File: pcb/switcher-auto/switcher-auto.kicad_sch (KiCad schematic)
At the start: 9 parts, among them J1 Conn_02x22_Top_Bottom, J2 Conn_02x22_Top_Bottom, J3 Conn_02x22_Top_Bottom, U1 CD74HC4067SM96, U2 CD74HC4067SM96, U3 CD74HC4067SM96, U4 CD74HC4067SM96, U5 CD74HC4067SM96, U6 CD74HC4067SM96

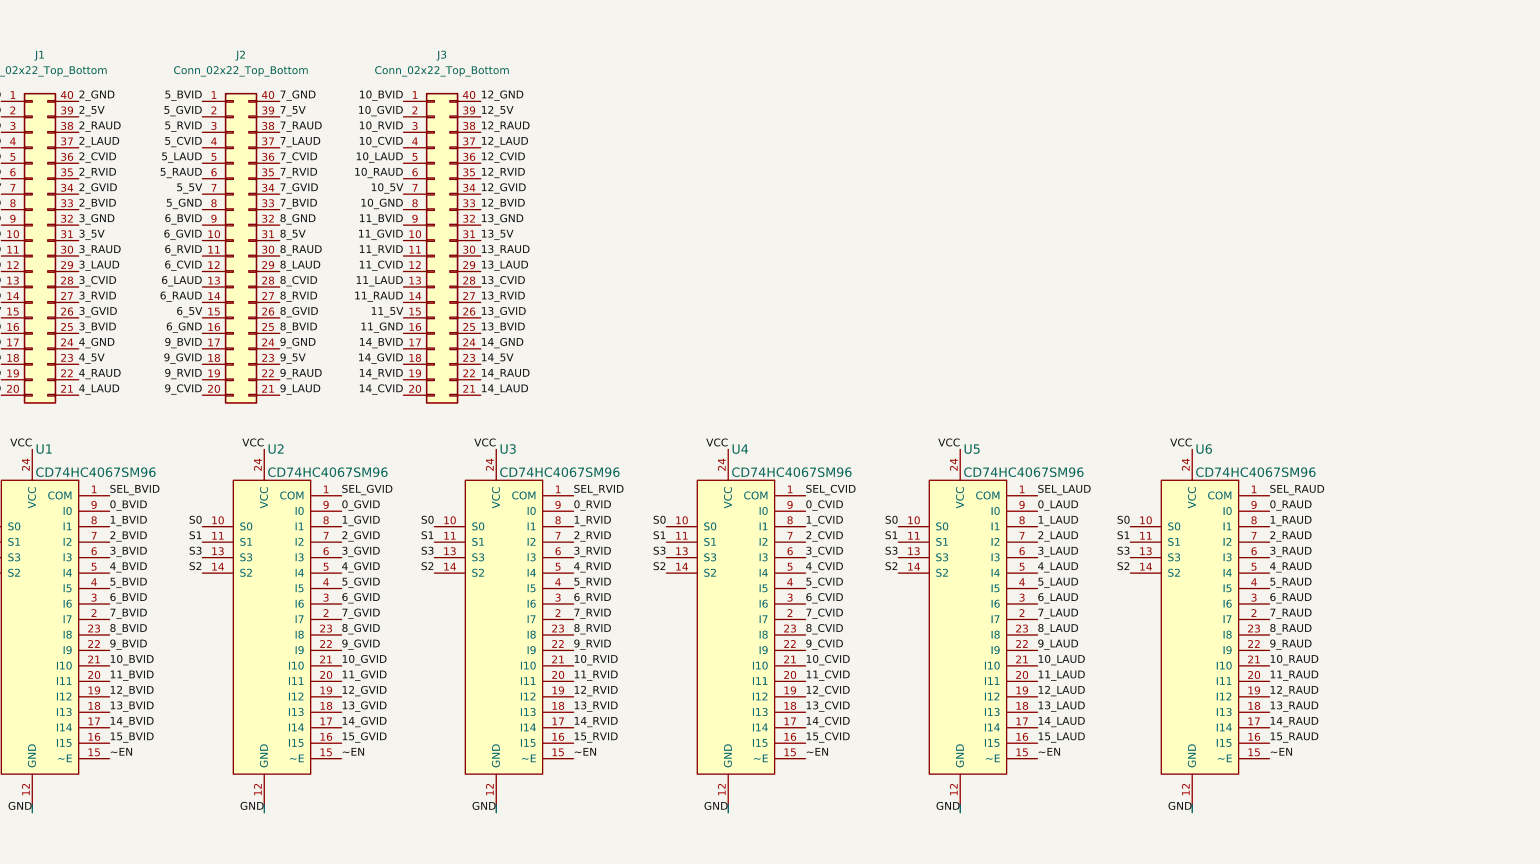
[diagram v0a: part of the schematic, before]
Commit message: autorouting 2layer switcher
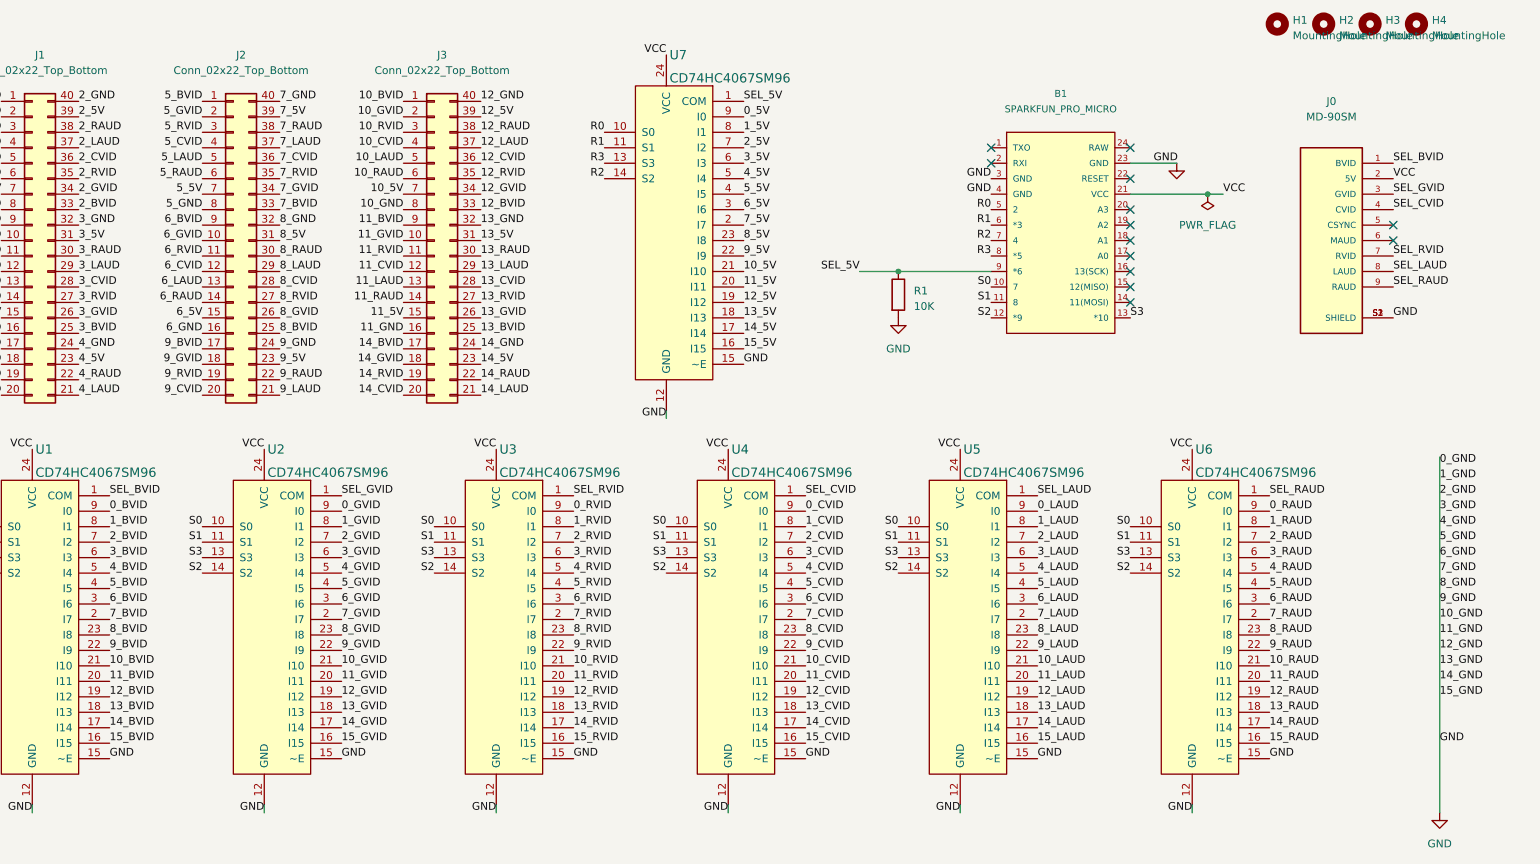
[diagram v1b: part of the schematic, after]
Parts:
- added B1: SPARKFUN_PRO_MICRO, SparkFun-Boards:SPARKFUN_PRO_MICRO, symbol SparkFun-Boards:SPARKFUN_PRO_MICRO
- added H1, H2, H3, H4: MountingHole, MountingHole:MountingHole_2.5mm, symbol Mechanical:MountingHole
- added J0: MD-90SM, DIN9:CUI_MD-90SM, symbol DIN9:MD-90SM
- added R1: 10K, Resistor_SMD:R_0805_2012Metric_Pad1.20x1.40mm_HandSolder, symbol Device:R
- added U7: CD74HC4067SM96, Package_SO:SSOP-24_5.3x8.2mm_P0.65mm, symbol dk_Interface-Analog-Switches-Multiplexers-Demultiplexers:CD74HC4067SM96
- U1, U2, U3, U4, U5, U6: footprint digikey-footprints:SSOP-24_W5.30mm -> Package_SO:SSOP-24_5.3x8.2mm_P0.65mm
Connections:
- net 0_GND is gone; now on net GND: J1.8 (Pin_8)
- net 10_GND is gone; now on net GND: J3.8 (Pin_8)
- net 11_GND is gone; now on net GND: J3.16 (Pin_16)
- net 12_GND is gone; now on net GND: J3.40 (Pin_40)
- net 13_GND is gone; now on net GND: J3.32 (Pin_32)
- net 14_GND is gone; now on net GND: J3.24 (Pin_24)
- net 1_GND is gone; now on net GND: J1.16 (Pin_16)
- net 2_GND is gone; now on net GND: J1.40 (Pin_40)
- net 3_GND is gone; now on net GND: J1.32 (Pin_32)
- net 4_GND is gone; now on net GND: J1.24 (Pin_24)
- net 5_GND is gone; now on net GND: J2.8 (Pin_8)
- net 6_GND is gone; now on net GND: J2.16 (Pin_16)
- net 7_GND is gone; now on net GND: J2.40 (Pin_40)
- net 8_GND is gone; now on net GND: J2.32 (Pin_32)
- net 9_GND is gone; now on net GND: J2.24 (Pin_24)
- net ~EN is gone; now on net GND: U1.15 (~E), U2.15 (~E), U3.15 (~E), U4.15 (~E), U5.15 (~E), U6.15 (~E)
- net 0_5V: now also U7.9 (I0)
- net 10_5V: now also U7.21 (I10)
- net 11_5V: now also U7.20 (I11)
- net 12_5V: now also U7.19 (I12)
- net 13_5V: now also U7.18 (I13)
- net 14_5V: now also U7.17 (I14)
- net 1_5V: now also U7.8 (I1)
- net 2_5V: now also U7.7 (I2)
- net 3_5V: now also U7.6 (I3)
- net 4_5V: now also U7.5 (I4)
- net 5_5V: now also U7.4 (I5)
- net 6_5V: now also U7.3 (I6)
- net 7_5V: now also U7.2 (I7)
- net 8_5V: now also U7.23 (I8)
- net 9_5V: now also U7.22 (I9)
- net GND: now also B1.23 (GND), B1.3 (GND), B1.4 (GND), J0.S1 (SHIELD), J0.S2 (SHIELD), J0.S3 (SHIELD), R1.2, U7.12 (GND), U7.15 (~E)
- net S0: now also B1.10 (7)
- net S1: now also B1.11 (8)
- net S2: now also B1.12 (*9)
- net S3: now also B1.13 (*10)
- net SEL_BVID: now also J0.1 (BVID)
- net SEL_CVID: now also J0.4 (CVID)
- net SEL_GVID: now also J0.3 (GVID)
- net SEL_LAUD: now also J0.8 (LAUD)
- net SEL_RAUD: now also J0.9 (RAUD)
- net SEL_RVID: now also J0.7 (RVID)
- net VCC: now also B1.21 (VCC), J0.2 (5V), U7.24 (VCC)
- new net 15_5V: U7.16 (I15)
- new net R0: B1.5 (2), U7.10 (S0)
- new net R1: B1.6 (*3), U7.11 (S1)
- new net R2: B1.7 (4), U7.14 (S2)
- new net R3: B1.8 (*5), U7.13 (S3)
- new net SEL_5V: B1.9 (*6), R1.1, U7.1 (COM)
- no-connect marks 0 -> 13

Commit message: Updates?
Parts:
- added R2: R, Resistor_SMD:R_1206_3216Metric_Pad1.30x1.75mm_HandSolder, symbol Device:R
- added SW1, SW2: SW_Push, Button_Switch_THT:SW_PUSH_6mm, symbol Switch:SW_Push
- R1: footprint Resistor_SMD:R_0805_2012Metric_Pad1.20x1.40mm_HandSolder -> Resistor_SMD:R_1206_3216Metric_Pad1.30x1.75mm_HandSolder
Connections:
- net GND: now also SW1.2, SW2.2; no longer U1.15 (~E), U2.15 (~E), U3.15 (~E), U4.15 (~E), U5.15 (~E), U6.15 (~E), U7.15 (~E)
- net SEL_5V: now also R2.1; no longer B1.9 (*6), R1.1
- net IE: now reaches B1.1 (TXO)
- net IE: now also U7.15 (~E)
- net at B1.14 (11(MOSI)): now also SW2.1
- net at B1.15 (12(MISO)): now also SW1.1
- net OE: now reaches B1.2 (RXI)
- net OE: now also U1.15 (~E), U2.15 (~E), U3.15 (~E), U4.15 (~E), U5.15 (~E), U6.15 (~E)
- new net: B1.9 (*6), R1.1, R2.2
- no-connect marks 13 -> 9
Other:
- moved on the sheet: R1
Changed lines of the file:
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@@
   (junction (at 231.14 46.99) (diameter 0) (color 0 0 0 0)
   )
-  (junction (at 180.34 59.69) (diameter 0) (color 0 0 0 0)
+  (junction (at 185.42 59.69) (diameter 0) (color 0 0 0 0)
   )
   (no_connect (at 218.44 59.69))
-  (no_connect (at 195.58 39.37))
-  (no_connect (at 218.44 64.77))
   (no_connect (at 261.62 54.61))
   (no_connect (at 218.44 39.37))
   (no_connect (at 218.44 54.61))
   (no_connect (at 218.44 52.07))
-  (no_connect (at 218.44 62.23))
   (no_connect (at 218.44 49.53))
-  (no_connect (at 195.58 41.91))
   (no_connect (at 261.62 52.07))
   (no_connect (at 218.44 57.15))
   (no_connect (at 218.44 44.45))
-  (wire (pts (xy 195.58 59.69) (xy 180.34 59.69))
+  (wire (pts (xy 195.58 59.69) (xy 185.42 59.69))
     (stroke (width 0) (type default))
   )
@@
     (stroke (width 0) (type default))
   )
+  (wire (pts (xy 218.44 62.23) (xy 224.79 62.23))
+    (stroke (width 0) (type default))
+  )
   (wire (pts (xy 228.6 148.59) (xy 228.6 147.32))
     (stroke (width 0) (type default))
   )
+  (wire (pts (xy 218.44 64.77) (xy 224.79 64.77))
+    (stroke (width 0) (type default))
+  )
   (wire (pts (xy 269.24 90.17) (xy 269.24 148.59))
     (stroke (width 0) (type default))
@@
     (stroke (width 0) (type default))
   )
-  (wire (pts (xy 180.34 59.69) (xy 173.99 59.69))
+  (wire (pts (xy 224.79 64.77) (xy 224.79 69.85))
+    (stroke (width 0) (type default))
+  )
+  (wire (pts (xy 185.42 59.69) (xy 184.15 59.69))
     (stroke (width 0) (type default))
   )
@@
     (stroke (width 0) (type default))
   )
+  (wire (pts (xy 176.53 59.69) (xy 168.91 59.69))
+    (stroke (width 0) (type default))
+  )
   (wire (pts (xy 190.5 148.59) (xy 190.5 147.32))
     (stroke (width 0) (type default))
   )
+  (wire (pts (xy 224.79 62.23) (xy 224.79 60.96))
+    (stroke (width 0) (type default))
+  )
   (wire (pts (xy 218.44 46.99) (xy 231.14 46.99))
     (stroke (width 0) (type default))
@@
     (effects (font (size 1.27 1.27)) (justify left bottom))
   )
+  (label "GND" (at 234.95 69.85 0) (fields_autoplaced)
+    (effects (font (size 1.27 1.27)) (justify left bottom))
+  )
   (label "0_5V" (at 154.94 34.29 0) (fields_autoplaced)
     (effects (font (size 1.27 1.27)) (justify left bottom))
@@
     (effects (font (size 1.27 1.27)) (justify right bottom))
   )
-  (label "GND" (at 127 139.7 0) (fields_autoplaced)
+  (label "OE" (at 127 139.7 0) (fields_autoplaced)
     (effects (font (size 1.27 1.27)) (justify left bottom))
   )
@@
     (effects (font (size 1.27 1.27)) (justify right bottom))
   )
-  (label "GND" (at 88.9 139.7 0) (fields_autoplaced)
+  (label "OE" (at 88.9 139.7 0) (fields_autoplaced)
+    (effects (font (size 1.27 1.27)) (justify left bottom))
+  )
+  (label "GND" (at 234.95 60.96 0) (fields_autoplaced)
     (effects (font (size 1.27 1.27)) (justify left bottom))
   )
@@
     (effects (font (size 1.27 1.27)) (justify left bottom))
   )
+  (label "OE" (at 195.58 41.91 180) (fields_autoplaced)
+    (effects (font (size 1.27 1.27)) (justify right bottom))
+  )
   (label "2_5V" (at 154.94 39.37 0) (fields_autoplaced)
     (effects (font (size 1.27 1.27)) (justify left bottom))
@@
     (effects (font (size 1.27 1.27)) (justify left bottom))
   )
-  (label "GND" (at 154.94 74.93 0) (fields_autoplaced)
+  (label "IE" (at 154.94 74.93 0) (fields_autoplaced)
     (effects (font (size 1.27 1.27)) (justify left bottom))
   )
@@
     (effects (font (size 1.27 1.27)) (justify left bottom))
   )
-  (label "GND" (at 203.2 139.7 0) (fields_autoplaced)
+  (label "OE" (at 203.2 139.7 0) (fields_autoplaced)
     (effects (font (size 1.27 1.27)) (justify left bottom))
   )
@@
     (effects (font (size 1.27 1.27)) (justify left bottom))
   )
-  (label "GND" (at 165.1 139.7 0) (fields_autoplaced)
+  (label "OE" (at 165.1 139.7 0) (fields_autoplaced)
     (effects (font (size 1.27 1.27)) (justify left bottom))
   )
@@
     (effects (font (size 1.27 1.27)) (justify left bottom))
   )
+  (label "IE" (at 195.58 39.37 180) (fields_autoplaced)
+    (effects (font (size 1.27 1.27)) (justify right bottom))
+  )
   (label "12_CVID" (at 165.1 129.54 0) (fields_autoplaced)
     (effects (font (size 1.27 1.27)) (justify left bottom))
@@
     (effects (font (size 1.27 1.27)) (justify right bottom))
   )
-  (label "GND" (at 50.8 139.7 0) (fields_autoplaced)
+  (label "OE" (at 50.8 139.7 0) (fields_autoplaced)
     (effects (font (size 1.27 1.27)) (justify left bottom))
   )
@@
     (effects (font (size 1.27 1.27)) (justify left bottom))
   )
-  (label "GND" (at 241.3 139.7 0) (fields_autoplaced)
+  (label "OE" (at 241.3 139.7 0) (fields_autoplaced)
     (effects (font (size 1.27 1.27)) (justify left bottom))
   )
@@
     )
   )
+  (symbol (lib_id "Switch:SW_Push") (at 229.87 69.85 0) (unit 1)
+    (in_bom yes) (on_board yes) (dnp no) (fields_autoplaced)
+    (property "Reference" "SW2" (at 229.87 63.5 0)
+      (effects (font (size 1.27 1.27)))
+    )
+    (property "Value" "SW_Push" (at 229.87 66.04 0)
+      (effects (font (size 1.27 1.27)))
+    )
+    (property "Footprint" "Button_Switch_THT:SW_PUSH_6mm" (at 229.87 64.77 0)
+      (effects (font (size 1.27 1.27)) hide)
+    )
+    (property "Datasheet" "~" (at 229.87 64.77 0)
+      (effects (font (size 1.27 1.27)) hide)
+    )
+    (pin "1")
+    (pin "2")
+    (instances
+      (project "switcher-auto"
+        (path "/e72d49f3-4a7e-4284-a905-90a44014e1f4"
+          (reference "SW2") (unit 1)
+        )
+      )
+    )
+  )
   (symbol (lib_id "Connector_Generic:Conn_02x20_Counter_Clockwise") (at 104.14 54.61 0) (unit 1)
     (in_bom yes) (on_board yes) (dnp no)
@@
     )
   )
-  (symbol (lib_id "power:GND") (at 180.34 67.31 0) (unit 1)
+  (symbol (lib_id "Device:R") (at 180.34 59.69 90) (unit 1)
     (in_bom yes) (on_board yes) (dnp no) (fields_autoplaced)
-    (property "Reference" "#PWR01" (at 180.34 73.66 0)
-      (effects (font (size 1.27 1.27)) hide)
-    )
-    (property "Value" "GND" (at 180.34 72.39 0)
+    (property "Reference" "R2" (at 180.34 54.61 90)
       (effects (font (size 1.27 1.27)))
     )
-    (property "Footprint" "" (at 180.34 67.31 0)
-      (effects (font (size 1.27 1.27)) hide)
-    )
-    (property "Datasheet" "" (at 180.34 67.31 0)
+    (property "Value" "R" (at 180.34 57.15 90)
+      (effects (font (size 1.27 1.27)))
+    )
+    (property "Footprint" "Resistor_SMD:R_1206_3216Metric_Pad1.30x1.75mm_HandSolder" (at 180.34 61.468 90)
+      (effects (font (size 1.27 1.27)) hide)
+    )
+    (property "Datasheet" "~" (at 180.34 59.69 0)
+      (effects (font (size 1.27 1.27)) hide)
+    )
+    (pin "1")
+    (pin "2")
+    (instances
+      (project "switcher-auto"
+        (path "/e72d49f3-4a7e-4284-a905-90a44014e1f4"
+          (reference "R2") (unit 1)
+        )
+      )
+    )
+  )
+  (symbol (lib_id "power:GND") (at 185.42 67.31 0) (unit 1)
+    (in_bom yes) (on_board yes) (dnp no) (fields_autoplaced)
+    (property "Reference" "#PWR01" (at 185.42 73.66 0)
+      (effects (font (size 1.27 1.27)) hide)
+    )
+    (property "Value" "GND" (at 185.42 72.39 0)
+      (effects (font (size 1.27 1.27)))
+    )
+    (property "Footprint" "" (at 185.42 67.31 0)
+      (effects (font (size 1.27 1.27)) hide)
+    )
+    (property "Datasheet" "" (at 185.42 67.31 0)
       (effects (font (size 1.27 1.27)) hide)
     )
@@
     )
   )
-  (symbol (lib_id "Device:R") (at 180.34 63.5 0) (unit 1)
+  (symbol (lib_id "Switch:SW_Push") (at 229.87 60.96 0) (unit 1)
     (in_bom yes) (on_board yes) (dnp no) (fields_autoplaced)
-    (property "Reference" "R1" (at 182.88 62.865 0)
+    (property "Reference" "SW1" (at 229.87 54.61 0)
+      (effects (font (size 1.27 1.27)))
+    )
+    (property "Value" "SW_Push" (at 229.87 57.15 0)
+      (effects (font (size 1.27 1.27)))
+    )
+    (property "Footprint" "Button_Switch_THT:SW_PUSH_6mm" (at 229.87 55.88 0)
+      (effects (font (size 1.27 1.27)) hide)
+    )
+    (property "Datasheet" "~" (at 229.87 55.88 0)
+      (effects (font (size 1.27 1.27)) hide)
+    )
+    (pin "1")
+    (pin "2")
+    (instances
+      (project "switcher-auto"
+        (path "/e72d49f3-4a7e-4284-a905-90a44014e1f4"
+          (reference "SW1") (unit 1)
+        )
+      )
+    )
+  )
+  (symbol (lib_id "Device:R") (at 185.42 63.5 0) (unit 1)
+    (in_bom yes) (on_board yes) (dnp no) (fields_autoplaced)
+    (property "Reference" "R1" (at 187.96 62.865 0)
       (effects (font (size 1.27 1.27)) (justify left))
     )
-    (property "Value" "10K" (at 182.88 65.405 0)
+    (property "Value" "10K" (at 187.96 65.405 0)
       (effects (font (size 1.27 1.27)) (justify left))
     )
-    (property "Footprint" "Resistor_SMD:R_0805_2012Metric_Pad1.20x1.40mm_HandSolder" (at 178.562 63.5 90)
-      (effects (font (size 1.27 1.27)) hide)
-    )
-    (property "Datasheet" "~" (at 180.34 63.5 0)
-      (effects (font (size 1.27 1.27)) hide)
-    )
+    (property "Footprint" "Resistor_SMD:R_1206_3216Metric_Pad1.30x1.75mm_HandSolder" (at 183.642 63.5 90)
+      (effects (font (size 1.27 1.27)) hide)
+    )
+    (property "Datasheet" "~" (at 185.42 63.5 0)
+      (effects (font (size 1.27 1.27)) hide)
+    )
